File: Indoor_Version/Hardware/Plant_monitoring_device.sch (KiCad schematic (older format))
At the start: 67 parts, among them J1 Barrel_Jack, J10 NXW-02, J11 NXW-03, J12 NXW-03, J13 NXW-03, J14 NXW-03, J2 SWO, J3 NXW-02, J4 NXW-02, J5 NXW-02, J6 NXW-02, J7 NXW-02, J8 NXW-02, J9 NXW-02, Q1 FDN308P, Q10 IRLML6346TRPBF, Q2 FDN308P, Q3 IRLML6346TRPBF, Q4 IRLML6346TRPBF, Q5 IRLML6346TRPBF, Q6 IRLML6346TRPBF, Q7 IRLML6346TRPBF, Q8 IRLML6346TRPBF, Q9 IRLML6346TRPBF, U1 STM32L031K6T6, U2 RN2483A, U3 AP2204RB-3.3TRG1, U4 SHT31

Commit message: Replaced STM32 with ESP32. Deleted the PCB.
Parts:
- removed A1: Antenna, MRS_Connectors:ANT_WIRE_THT, symbol MRS_Communication:Antenna
- removed BAT1: Battery, MRS_Connectors:BatteryHolder_Keystone_2468_2xAAA, symbol MRS_Power:Battery
- removed C13, C22: 0.1uF, MRS_Passives:C0603, symbol MRS_Passives:C
- removed C21: 1uF, MRS_Passives:C0603, symbol MRS_Passives:C
- removed J2: SWO, MRS_Connectors:Header_1x05_P2.54mm, symbol MRS_Connectors:Header_1x5
- removed Q1, Q2: FDN308P, MRS_SOT:SOT-23, symbol MRS_Transistors:FDN308P
- removed R1, R2: 10k, MRS_Passives:R0603, symbol MRS_Passives:R
- removed SB1, SB2, SB3, SB4, SB5, SB6: SolderBridge, MRS_Connectors:SB0603, symbol MRS_Connectors:SolderBridge
- removed U1: STM32L031K6T6, MRS_QFP:LQFP-32_7x7mm_P0.8mm, symbol MRS_MCUs:STM32L031K6T6
- removed U2: RN2483A, MRS_Communication:RN2483A, symbol MRS_Communication:RN2483A
- added U1: ESP32-WROOM, MRS_Communication:ESP32-WROOM, symbol MRS_MCUs:ESP32-WROOM
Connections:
- net labels removed: LORA_nRESET, PA11, PF0, PF1, VDD, VDDA
- wire segments 163 -> 118
- no-connect marks 33 -> 3
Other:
- note removed: "2x AAA"
- note removed: "50 Ohm"
- note removed: "LoRa Module"
- note removed: "VCC - Power for MCU\nVDD - Power for LoRa\nVDDA - Power for Sensors"
- note removed: "VDDA"
- note removed: "VDDIO"
- moved on the sheet: C11, C12

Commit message: Created outline of the PCB and basic layout of connectors. Created schematic and PCB layout of the buck convertor.
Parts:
- removed U3: AP2204RB-3.3TRG1, MRS_SOT:SOT-89, symbol MRS_Power_Management:AP2204RB-3.3TRG1
- added C21: 10uF, MRS_Passives:C1210, symbol MRS_Passives:C
- added C22: 1uF, MRS_Passives:C0603, symbol MRS_Passives:C
- added C35: 10nF, MRS_Passives:C0603, symbol MRS_Passives:C
- added D1, D31: MBR230LSFT1G, MRS_Diodes:SOD-123, symbol MRS_Diodes:Diode_Schottky
- added H4: Mounting_hole_unplated_3,2mm, MRS_Mechanical:Mounting_hole_unplated_3,2mm, symbol MRS_Mechanical:Mounting_hole_unplated_3,2mm
- added J2: Header_1x6, MRS_Connectors:Header_1x06_P2.54mm, symbol MRS_Connectors:Header_1x6
- added L31: 2.2uH, MRS_Passives:L1210, symbol MRS_Passives:L
- added R31: 10k, MRS_Passives:R0603, symbol MRS_Passives:R
- added R32: 49k9, MRS_Passives:R0603, symbol MRS_Passives:R
- added R33: 15k8, MRS_Passives:R0603, symbol MRS_Passives:R
- added U2: MCP3424-E_SL, MRS_SO:SOIC-14, symbol MRS_Sensors:MCP3424-E_SL
- added U3: AOZ1280, MRS_SOT:SOT-23-6, symbol MRS_Power_Management:AOZ1280
- C31, C33: footprint MRS_Passives:C0603 -> MRS_Passives:C1210
- J10, J3, J4, J5, J6, J7, J8, J9: value NXW-02 -> A2501WR-2P1; footprint MRS_Connectors:NXW-02 -> MRS_Connectors:A2501WR-2P1
- J11, J12, J13, J14: value NXW-03 -> A2501WR-3P1; footprint MRS_Connectors:NXW-03 -> MRS_Connectors:A2501WR-3P1
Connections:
- net labels added: +3V3, EN, IO0, PUMP1, PUMP2, PUMP3, PUMP4, SIG_PWM
- net labels removed: ADC_BAT, BAT_LO, COMM_ENA, NRST, SWCLK, SWDIO, VCC
- wire segments 118 -> 155
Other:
- note added: "tantal"
- note removed: "3V3"
- note removed: "VDD"
- moved on the sheet: C11, C12, C31, C32, C33, C34, J1, J11, J12, J13, J14, LD13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

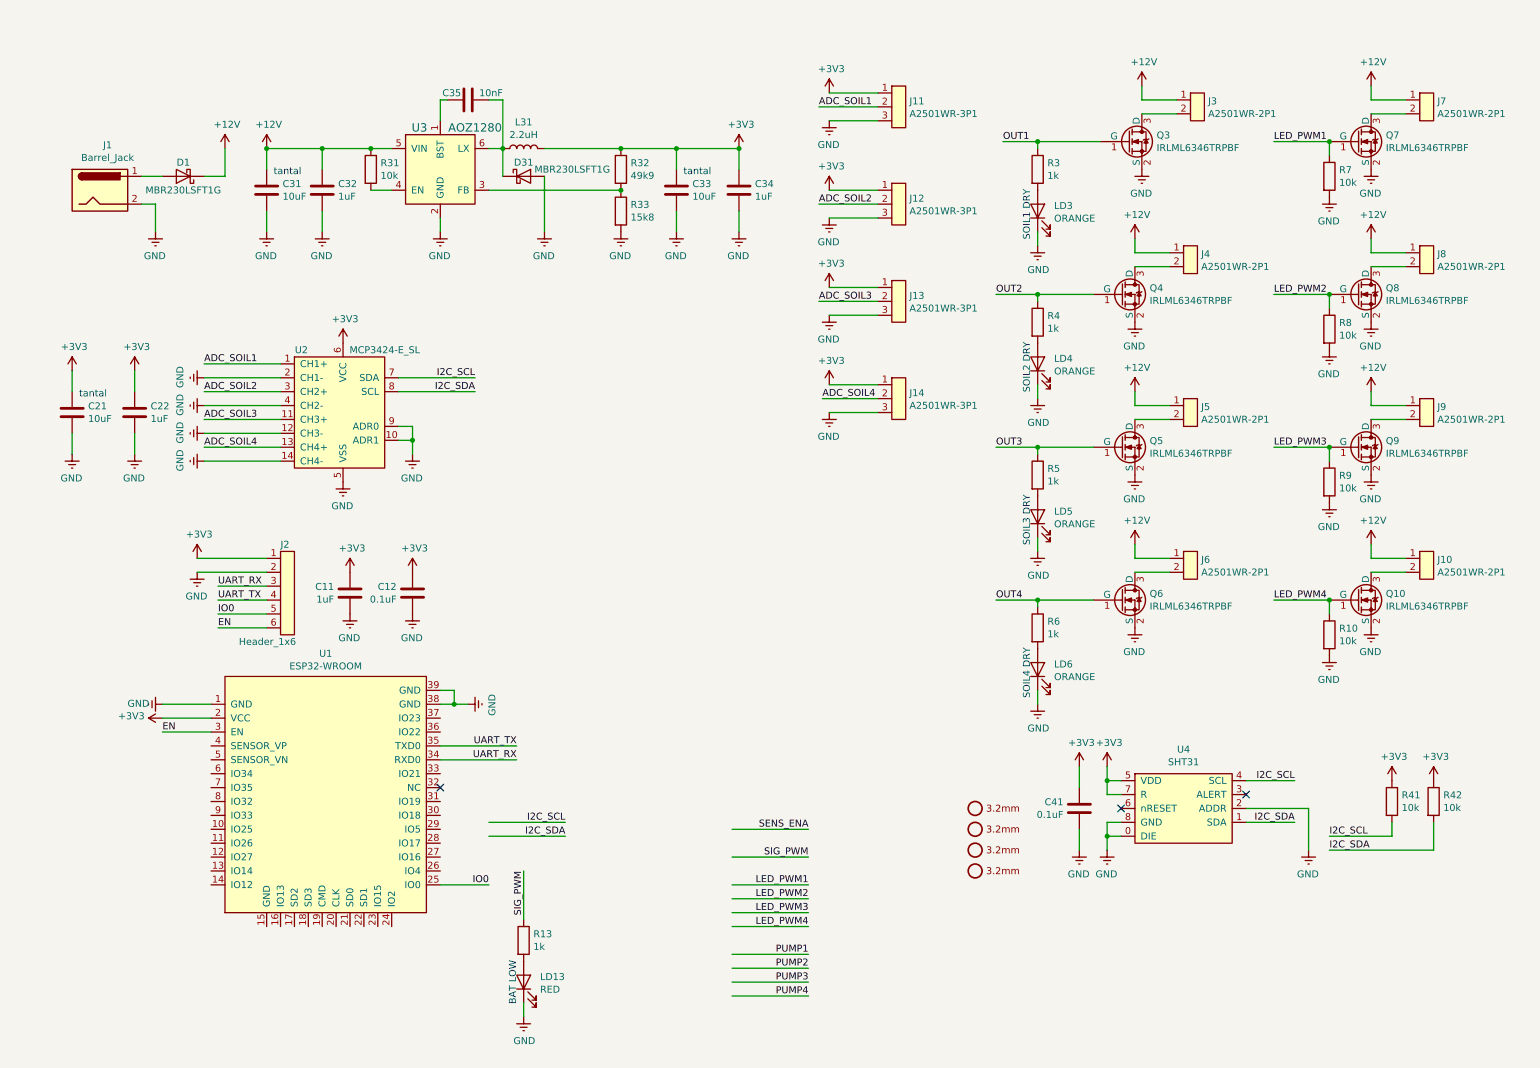
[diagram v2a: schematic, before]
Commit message: Finished design of the indoor version of the gardener. Generated gerbers.
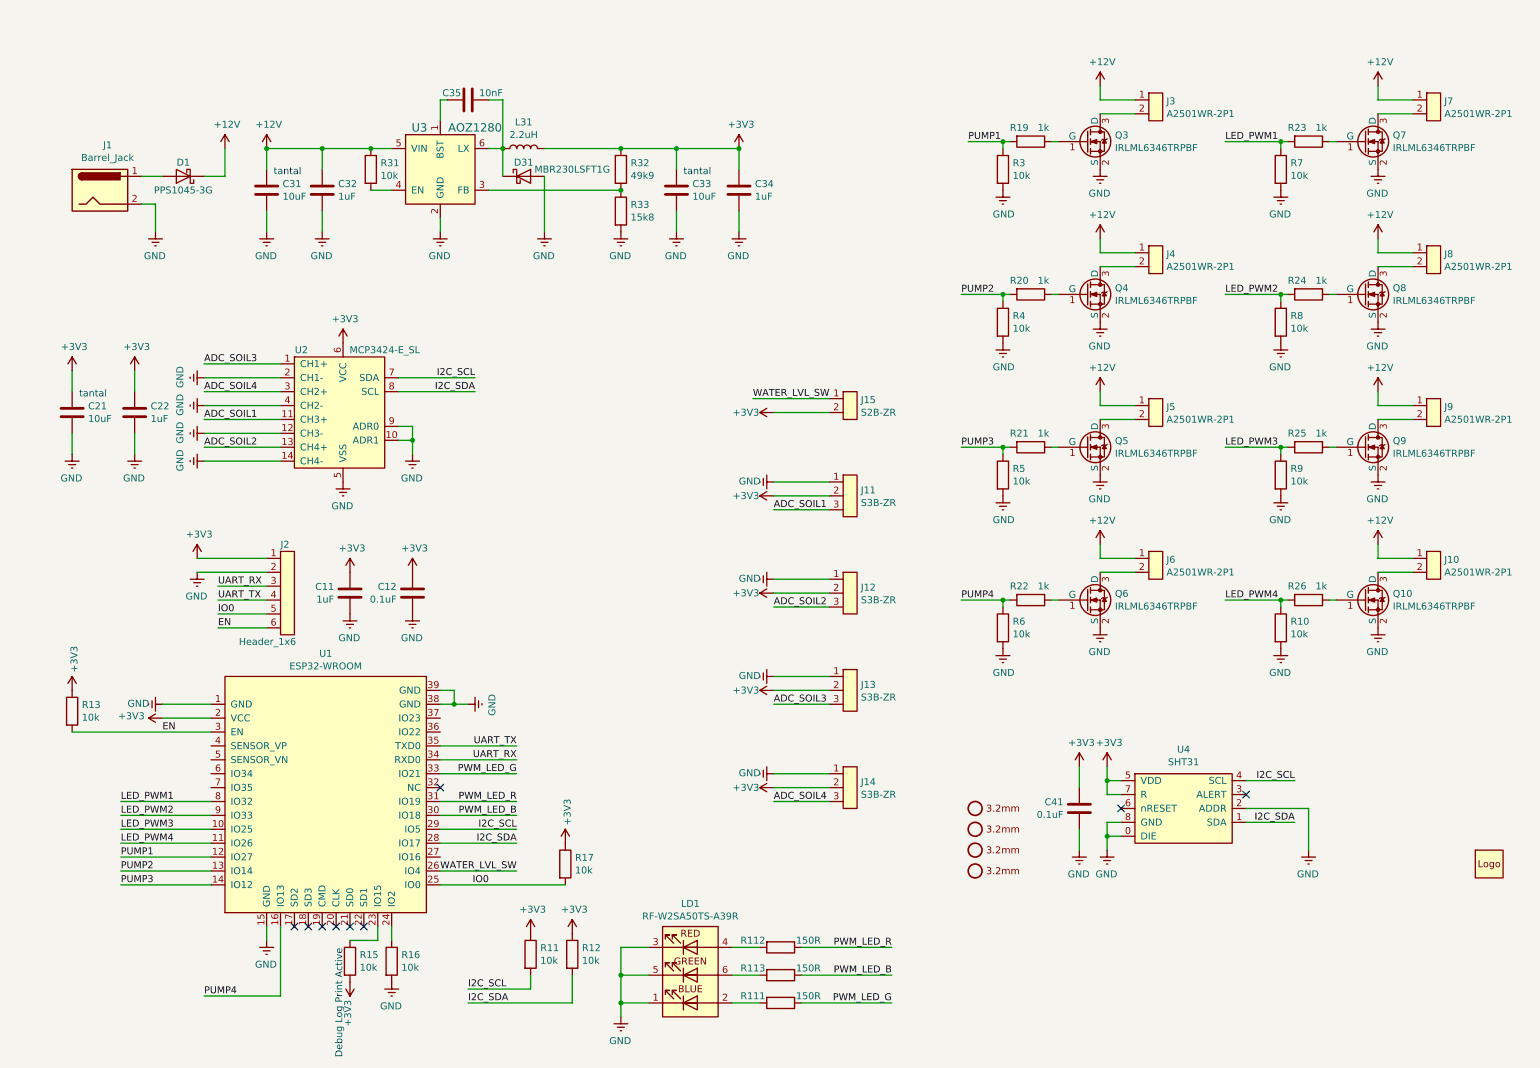
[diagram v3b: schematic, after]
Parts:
- removed LD13: RED, MRS_Diodes:LED_0805, symbol MRS_Diodes:Diode_LED_0805
- removed LD3, LD4, LD5, LD6: ORANGE, MRS_Diodes:LED_0805, symbol MRS_Diodes:Diode_LED_0805
- added H111: Mr_Gardener_Logo_Small, Logos:mrg_gardener_12mm, symbol Mr_Gardener_Logos:Mr_Gardener_Logo_Small
- added J15: S2B-ZR, MRS_Connectors:S2B-ZR, symbol MRS_Connectors:NXW-02
- added LD1: RF-W2SA50TS-A39R, MRS_Diodes:RF-W2SA50TS-A39R, symbol MRS_Diodes:RF-W2SA50TS-A39R
- added R111, R112, R113: 150R, MRS_Passives:R0603, symbol MRS_Passives:R
- added R15, R16, R17: 10k, MRS_Passives:R0603, symbol MRS_Passives:R
- added R19, R20, R21, R22, R23, R24, R25, R26: 1k, MRS_Passives:R0603, symbol MRS_Passives:R
- D1: value MBR230LSFT1G -> PPS1045-3G; footprint MRS_Diodes:SOD-123 -> MRS_TO:TO-277-3; TME MBR230LSFT1G -> PPS1045-3G-DIO
- J10, J3, J4, J5, J6, J7, J8, J9: TME NXW-02, NXG-02, NXG-T -> NXW-02K, NXG-02, NXG-T
- J11, J12, J13, J14: value A2501WR-3P1 -> S3B-ZR; footprint MRS_Connectors:A2501WR-3P1 -> MRS_Connectors:S3B-ZR; TME NXW-03, NXG-03, NXG-T -> S3B-ZR
- R13, R3, R4, R5, R6: value 1k -> 10k; TME WF06P-1K-5% -> WF06P-10K-5%
- renumbered R41 to R11, R42 to R12
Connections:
- net labels added: PWM_LED_B, PWM_LED_G, PWM_LED_R, WATER_LVL_SW
- net labels removed: OUT1, OUT2, OUT3, OUT4, SENS_ENA, SIG_PWM
- wire segments 155 -> 182
- no-connect marks 3 -> 9
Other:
- note added: "Debug Log Print Active"
- note removed: "BAT LOW"
- note removed: "SOIL1 DRY"
- note removed: "SOIL2 DRY"
- note removed: "SOIL3 DRY"
- note removed: "SOIL4 DRY"
- moved on the sheet: J10, J11, J12, J13, J14, J3, J4, J5, J6, J7, J8, J9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

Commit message: Minor changes.
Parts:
- C11, C12, C21, C22, C31, C32, C33, C34, C35, C41: symbol MRS_Passives:C -> Plant_monitoring_device-rescue:C-MRS_Passives
- D1, D31: symbol MRS_Diodes:Diode_Schottky -> Plant_monitoring_device-rescue:Diode_Schottky-MRS_Diodes
- H1, H2, H3, H4: symbol MRS_Mechanical:Mounting_hole_unplated_3,2mm -> Plant_monitoring_device-rescue:Mounting_hole_unplated_3,2mm-MRS_Mechanical
- H111: symbol Mr_Gardener_Logos:Mr_Gardener_Logo_Small -> Plant_monitoring_device-rescue:Mr_Gardener_Logo_Small-Mr_Gardener_Logos
- J1: symbol MRS_Connectors:Barrel_Jack -> Plant_monitoring_device-rescue:Barrel_Jack-MRS_Connectors
- J10, J15, J3, J4, J5, J6, J7, J8, J9: symbol MRS_Connectors:NXW-02 -> Plant_monitoring_device-rescue:NXW-02-MRS_Connectors
- J11, J12, J13, J14: symbol MRS_Connectors:NXW-03 -> Plant_monitoring_device-rescue:NXW-03-MRS_Connectors
- J2: symbol MRS_Connectors:Header_1x6 -> Plant_monitoring_device-rescue:Header_1x6-MRS_Connectors
- L31: symbol MRS_Passives:L -> Plant_monitoring_device-rescue:L-MRS_Passives
- LD1: symbol MRS_Diodes:RF-W2SA50TS-A39R -> Plant_monitoring_device-rescue:RF-W2SA50TS-A39R-MRS_Diodes
- Q10, Q3, Q4, Q5, Q6, Q7, Q8, Q9: symbol MRS_Transistors:IRLML6346TRPBF -> Plant_monitoring_device-rescue:IRLML6346TRPBF-MRS_Transistors
- R10, R11, R111, R112, R113, R12, R13, R15, R16, R17, R19, R20, R21, R22, R23, R24, R25, R26, R3, R31, R32, R33, R4, R5, R6, R7, R8, R9: symbol MRS_Passives:R -> Plant_monitoring_device-rescue:R-MRS_Passives
- U1: symbol MRS_MCUs:ESP32-WROOM -> Plant_monitoring_device-rescue:ESP32-WROOM-MRS_MCUs
- U2: symbol MRS_Sensors:MCP3424-E_SL -> Plant_monitoring_device-rescue:MCP3424-E_SL-MRS_Sensors
- U3: symbol MRS_Power_Management:AOZ1280 -> Plant_monitoring_device-rescue:AOZ1280-MRS_Power_Management
- U4: symbol MRS_Sensors:SHT31 -> Plant_monitoring_device-rescue:SHT31-MRS_Sensors
